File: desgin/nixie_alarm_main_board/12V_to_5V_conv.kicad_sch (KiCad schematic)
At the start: 9 parts, among them IC3 TPS563219ADDFR

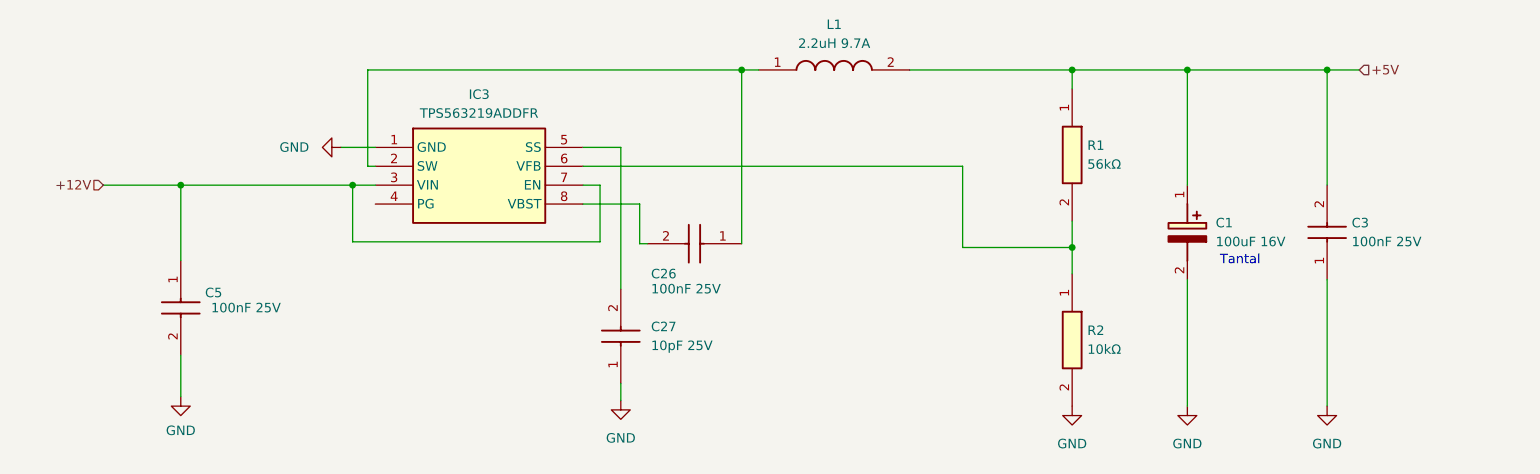
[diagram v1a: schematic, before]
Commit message: new conv capacitors
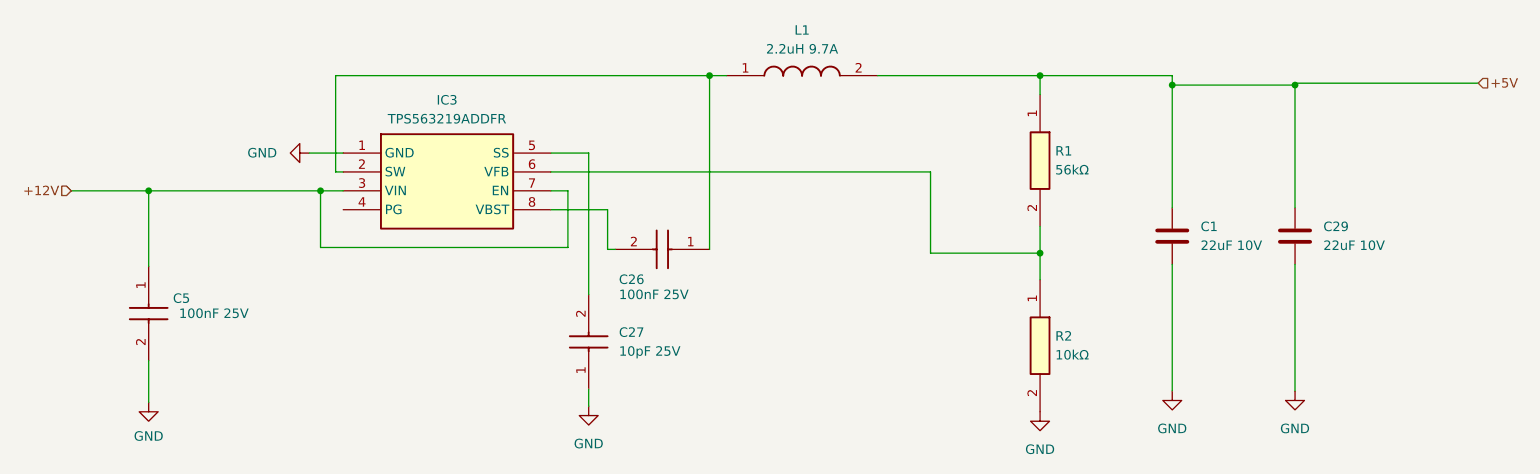
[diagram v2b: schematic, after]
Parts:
- removed C1: 100uF 16V, CAPPM7344X310N, symbol SamacSys_Parts:TAJD107K016RNJ
- removed C3: 100nF 25V, Capacitor_SMD:C_0805_2012Metric_Pad1.18x1.45mm_HandSolder, symbol SamacSys_Parts:GRM033R71E101KA01J
- added C1, C29: 22uF 10V, Capacitor_SMD:C_0805_2012Metric_Pad1.18x1.45mm_HandSolder, symbol Device:C
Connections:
- net +5V: now also C1.1, C29.1
- net GND: now also C1.2, C29.2
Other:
- note removed: "Tantal"
- moved on the sheet: C26, C27, C5, IC3, L1, R1, R2

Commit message: marged with board v2
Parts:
- C27: value 10pF 25V -> 10nF 25V
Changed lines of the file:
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@@
 		)
 		(instances
-			(project ""
+			(project "nixie_alarm_main_board"
 				(path "/a0d555d7-39a0-4a98-b831-70d97d0aa5a1/0943c442-6dd2-4b0d-a6a3-5c379f0041bb"
 					(reference "C1")
@@
 		(fields_autoplaced yes)
 		(property "Reference" "C27"
-			(at 144.018 92.9639 90)
+			(at 143.51 92.9639 90)
 			(effects
 				(font
@@
 			)
 		)
-		(property "Value" "10pF 25V"
-			(at 144.018 95.5039 90)
-			(effects
-				(font
+		(property "Value" "10nF 25V"
+			(at 143.51 95.5039 90)
+			(effects
+				(font
